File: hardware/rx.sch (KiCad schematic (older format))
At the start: 18 parts, among them J4 SMA, U22 TRF37A73, U23 SKY65404

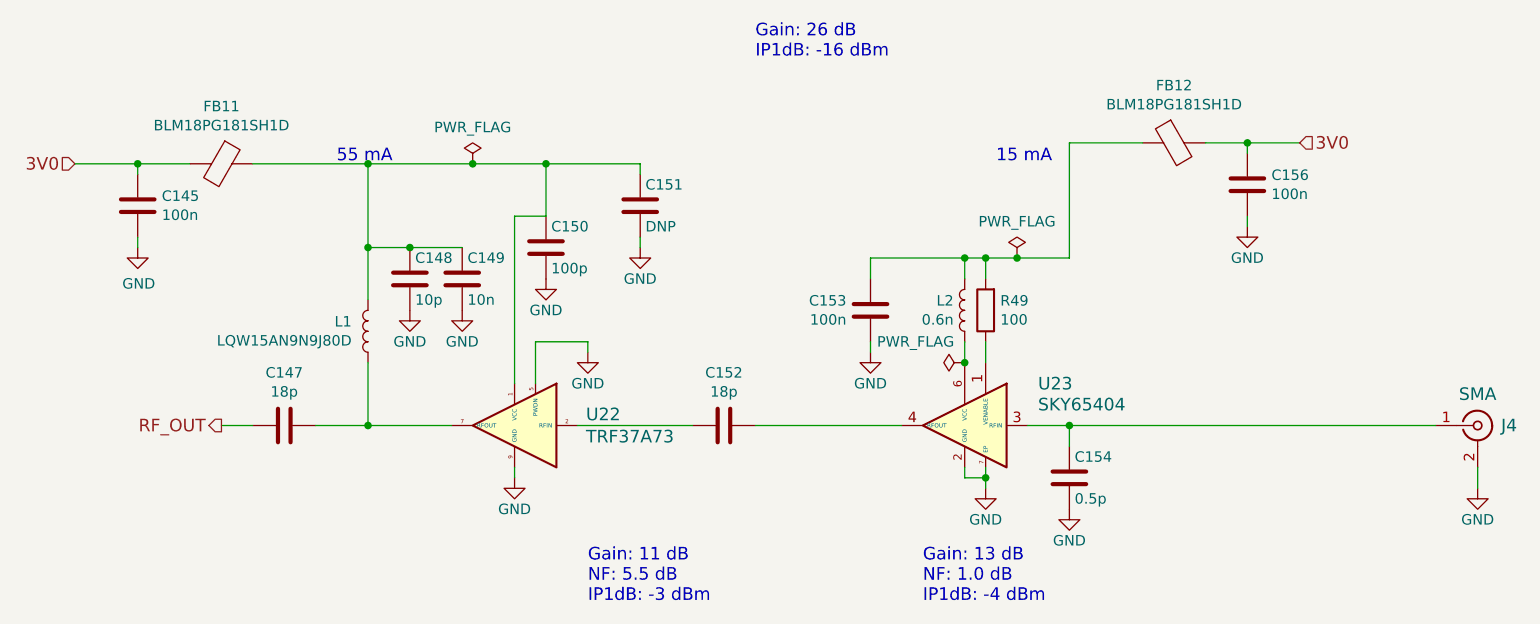
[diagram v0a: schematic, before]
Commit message: Completed receivers.
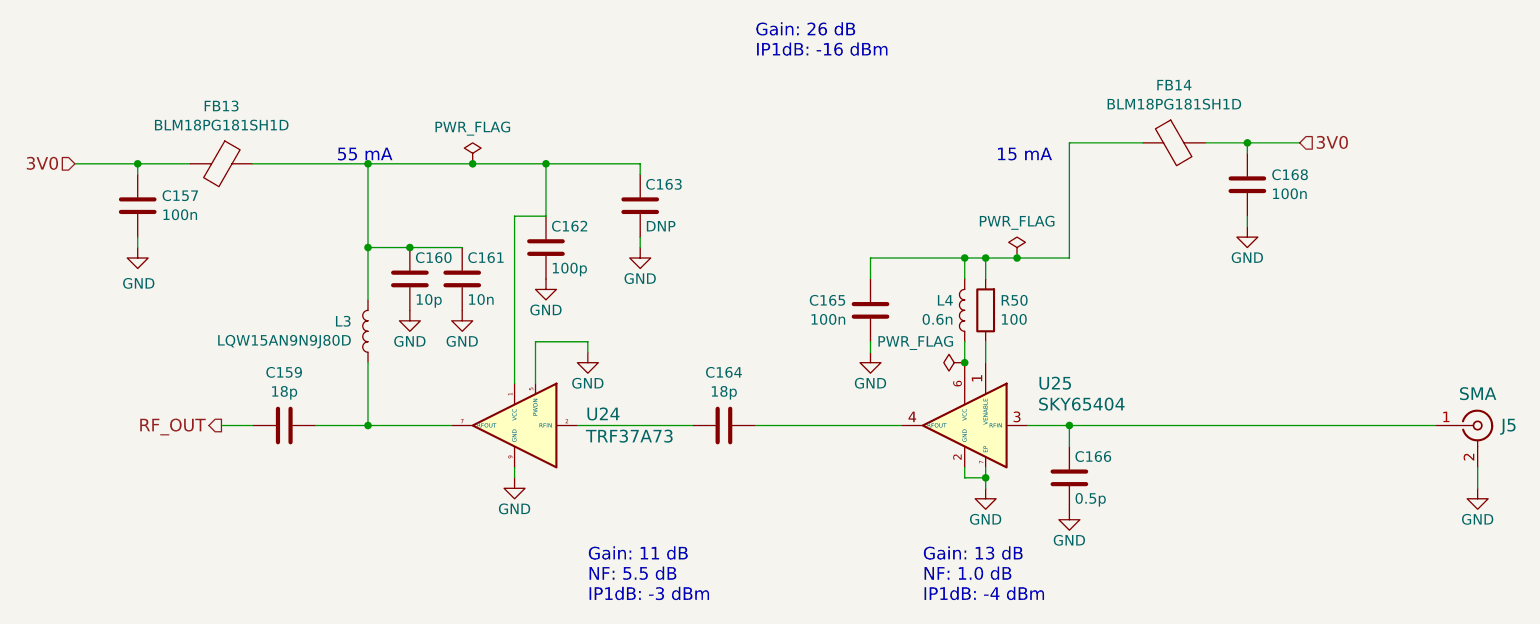
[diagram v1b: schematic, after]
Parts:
- C154: MFN C1005C0G1H0R5B050BA -> 500R07S0R5BV4T
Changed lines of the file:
@@
 $Descr A4 11693 8268
 encoding utf-8
-Sheet 6 10
+Sheet 7 10
 Title ""
 Date ""
@@
 AR Path="/59396B97/593BC199" Ref="U23"  Part="1"
 AR Path="/593D90BA/593BC199" Ref="U25"  Part="1"
-F 0 "U23" H 6550 4150 60  0000 R CNN
+F 0 "U25" H 6550 4150 60  0000 R CNN
 F 1 "SKY65404" H 6550 4050 60  0000 R CNN
 F 2 "Package_DFN_QFN:Skyworks_DFN-6-1EP_1.5x1.5mm_P0.5mm_EP0.7x1.2mm" H 6750 3950 60  0001 C CNN
@@
 AR Path="/59396B97/593BC25F" Ref="#PWR0158"  Part="1"
 AR Path="/593D90BA/593BC25F" Ref="#PWR0172"  Part="1"
-F 0 "#PWR0158" H 6800 4000 50  0001 C CNN
+F 0 "#PWR0172" H 6800 4000 50  0001 C CNN
 F 1 "GND" H 6800 4100 50  0000 C CNN
 F 2 "" H 6800 4250 60  0000 C CNN
@@
 AR Path="/59396B97/593BC396" Ref="R49"  Part="1"
 AR Path="/593D90BA/593BC396" Ref="R50"  Part="1"
-F 0 "R49" H 6730 3354 50  0000 R CNN
+F 0 "R50" H 6730 3354 50  0000 R CNN
 F 1 "100" H 6730 3445 50  0000 R CNN
 F 2 "Resistor_SMD:R_0402_1005Metric" V 6730 3400 30  0001 C CNN
@@
 AR Path="/59396B97/593BC695" Ref="L2"  Part="1"
 AR Path="/593D90BA/593BC695" Ref="L4"  Part="1"
-F 0 "L2" H 6753 3354 50  0000 L CNN
+F 0 "L4" H 6753 3354 50  0000 L CNN
 F 1 "0.6n" H 6753 3445 50  0000 L CNN
 F 2 "Inductor_SMD:L_0402_1005Metric" H 6700 3400 60  0001 C CNN
@@
 AR Path="/59396B97/593BC767" Ref="C153"  Part="1"
 AR Path="/593D90BA/593BC767" Ref="C165"  Part="1"
-F 0 "C153" H 6135 3446 50  0000 R CNN
+F 0 "C165" H 6135 3446 50  0000 R CNN
 F 1 "100n" H 6135 3355 50  0000 R CNN
 F 2 "Capacitor_SMD:C_0402_1005Metric" H 6288 3250 30  0001 C CNN
@@
 AR Path="/59396B97/593BC7DB" Ref="#PWR0157"  Part="1"
 AR Path="/593D90BA/593BC7DB" Ref="#PWR0171"  Part="1"
-F 0 "#PWR0157" H 6250 3350 50  0001 C CNN
+F 0 "#PWR0171" H 6250 3350 50  0001 C CNN
 F 1 "GND" H 6250 3450 50  0000 C CNN
 F 2 "" H 6250 3600 60  0000 C CNN
@@
 AR Path="/59396B97/593BCCCA" Ref="J4"  Part="1"
 AR Path="/593D90BA/593BCCCA" Ref="J5"  Part="1"
-F 0 "J4" H 9300 3950 60  0000 C CNN
+F 0 "J5" H 9300 3950 60  0000 C CNN
 F 1 "SMA" H 9150 4100 60  0000 C CNN
 F 2 "fmcw:CONSMA003.062" H 9150 3950 60  0001 C CNN
@@
 AR Path="/59396B97/593BCD59" Ref="#PWR0162"  Part="1"
 AR Path="/593D90BA/593BCD59" Ref="#PWR0176"  Part="1"
-F 0 "#PWR0162" H 9150 4000 50  0001 C CNN
+F 0 "#PWR0176" H 9150 4000 50  0001 C CNN
 F 1 "GND" H 9150 4100 50  0000 C CNN
 F 2 "" H 9150 4250 60  0000 C CNN
@@
 AR Path="/59396B97/593BCEBC" Ref="C154"  Part="1"
 AR Path="/593D90BA/593BCEBC" Ref="C166"  Part="1"
-F 0 "C154" H 7225 4300 50  0000 L CNN
+F 0 "C166" H 7225 4300 50  0000 L CNN
 F 1 "0.5p" H 7225 4100 50  0000 L CNN
 F 2 "Capacitor_SMD:C_0402_1005Metric" H 7238 4050 30  0001 C CNN
 F 3 "" H 7200 4200 60  0000 C CNN
-F 4 "C1005C0G1H0R5B050BA" H -1250 0   50  0001 C CNN "MFN"
+F 4 "500R07S0R5BV4T" H -1250 0   50  0001 C CNN "MFN"
 	1    7200 4200
 	1    0    0    -1
@@
 AR Path="/59396B97/593BCF37" Ref="#PWR0159"  Part="1"
 AR Path="/593D90BA/593BCF37" Ref="#PWR0173"  Part="1"
-F 0 "#PWR0159" H 7200 4100 50  0001 C CNN
+F 0 "#PWR0173" H 7200 4100 50  0001 C CNN
 F 1 "GND" H 7200 4200 50  0000 C CNN
 F 2 "" H 7200 4350 60  0000 C CNN
@@
 AR Path="/59396B97/593BD4EF" Ref="C152"  Part="1"
 AR Path="/593D90BA/593BD4EF" Ref="C164"  Part="1"
-F 0 "C152" V 5298 3950 50  0000 C CNN
+F 0 "C164" V 5298 3950 50  0000 C CNN
 F 1 "18p" V 5389 3950 50  0000 C CNN
 F 2 "Capacitor_SMD:C_0402_1005Metric" H 5588 3800 30  0001 C CNN
@@
 AR Path="/59396B97/593BD727" Ref="#PWR0153"  Part="1"
 AR Path="/593D90BA/593BD727" Ref="#PWR0167"  Part="1"
-F 0 "#PWR0153" H 4550 3950 50  0001 C CNN
+F 0 "#PWR0167" H 4550 3950 50  0001 C CNN
 F 1 "GND" H 4550 4050 50  0000 C CNN
 F 2 "" H 4550 4200 60  0000 C CNN
@@
 AR Path="/59396B97/593BD8E8" Ref="L1"  Part="1"
 AR Path="/593D90BA/593BD8E8" Ref="L3"  Part="1"
-F 0 "L1" H 3928 3454 50  0000 L CNN
+F 0 "L3" H 3928 3454 50  0000 L CNN
 F 1 "LQW15AN9N9J80D" H 3928 3545 50  0000 L CNN
 F 2 "Inductor_SMD:L_0402_1005Metric" H 3850 3500 60  0001 C CNN
@@
 AR Path="/59396B97/593BDA25" Ref="C148"  Part="1"
 AR Path="/593D90BA/593BDA25" Ref="C160"  Part="1"
-F 0 "C148" H 4075 3350 50  0000 L CNN
+F 0 "C160" H 4075 3350 50  0000 L CNN
 F 1 "10p" H 4075 3150 50  0000 L CNN
 F 2 "Capacitor_SMD:C_0402_1005Metric" H 4088 3100 30  0001 C CNN
@@
 AR Path="/59396B97/593BDABD" Ref="#PWR0151"  Part="1"
 AR Path="/593D90BA/593BDABD" Ref="#PWR0165"  Part="1"
-F 0 "#PWR0151" H 4050 3150 50  0001 C CNN
+F 0 "#PWR0165" H 4050 3150 50  0001 C CNN
 F 1 "GND" H 4050 3250 50  0000 C CNN
 F 2 "" H 4050 3400 60  0000 C CNN
@@
 AR Path="/59396B97/593BDF98" Ref="C147"  Part="1"
 AR Path="/593D90BA/593BDF98" Ref="C159"  Part="1"
-F 0 "C147" V 3198 3950 50  0000 C CNN
+F 0 "C159" V 3198 3950 50  0000 C CNN
 F 1 "18p" V 3289 3950 50  0000 C CNN
 F 2 "Capacitor_SMD:C_0402_1005Metric" H 3488 3800 30  0001 C CNN
@@
 AR Path="/593D90BA/59751767" Ref="FB13"  Part="1"
 AR Path="/59396B97/59751767" Ref="FB11"  Part="1"
-F 0 "FB11" V 2876 2700 50  0000 C CNN
+F 0 "FB13" V 2876 2700 50  0000 C CNN
 F 1 "BLM18PG181SH1D" V 2967 2700 50  0000 C CNN
 F 2 "Inductor_SMD:L_0603_1608Metric" H 3150 2700 60  0001 C CNN
@@
 AR Path="/593D90BA/59751D28" Ref="C163"  Part="1"
 AR Path="/59396B97/59751D28" Ref="C151"  Part="1"
-F 0 "C151" H 5175 3000 50  0000 L CNN
+F 0 "C163" H 5175 3000 50  0000 L CNN
 F 1 "DNP" H 5175 2800 50  0000 L CNN
 F 2 "Capacitor_SMD:C_0603_1608Metric" H 5188 2750 30  0001 C CNN
@@
 AR Path="/593D90BA/59751D9B" Ref="#PWR0170"  Part="1"
 AR Path="/59396B97/59751D9B" Ref="#PWR0156"  Part="1"
-F 0 "#PWR0156" H 5150 2850 50  0001 C CNN
+F 0 "#PWR0170" H 5150 2850 50  0001 C CNN
 F 1 "GND" H 5150 2950 50  0000 C CNN
 F 2 "" H 5150 3100 60  0000 C CNN
@@
 AR Path="/593D90BA/597527FA" Ref="FB14"  Part="1"
 AR Path="/59396B97/597527FA" Ref="FB12"  Part="1"
-F 0 "FB12" V 7426 2600 50  0000 C CNN
+F 0 "FB14" V 7426 2600 50  0000 C CNN
 F 1 "BLM18PG181SH1D" V 7517 2600 50  0000 C CNN
 F 2 "Inductor_SMD:L_0603_1608Metric" H 7700 2600 60  0001 C CNN
@@
 AR Path="/59396B97/59752CE4" Ref="#PWR0161"  Part="1"
 AR Path="/593D90BA/59752CE4" Ref="#PWR0175"  Part="1"
-F 0 "#PWR0161" H 8050 2750 50  0001 C CNN
+F 0 "#PWR0175" H 8050 2750 50  0001 C CNN
 F 1 "GND" H 8050 2850 50  0000 C CNN
 F 2 "" H 8050 3000 60  0000 C CNN
@@
 AR Path="/593D90BA/597605DF" Ref="U24"  Part="1"
 AR Path="/597605DF" Ref="U?"  Part="1"
-F 0 "U22" H 4409 4003 60  0000 R CNN
+F 0 "U24" H 4409 4003 60  0000 R CNN
 F 1 "TRF37A73" H 4409 3897 60  0000 R CNN
 F 2 "Package_SON:WSON-8-1EP_2x2mm_P0.5mm_EP0.9x1.6mm" H 4450 3900 60  0001 C CNN
@@
 AR Path="/59396B97/59761DBE" Ref="C150"  Part="1"
 AR Path="/593D90BA/59761DBE" Ref="C162"  Part="1"
-F 0 "C150" H 4725 3200 50  0000 L CNN
+F 0 "C162" H 4725 3200 50  0000 L CNN
 F 1 "100p" H 4725 3000 50  0000 L CNN
 F 2 "Capacitor_SMD:C_0402_1005Metric" H 4738 2950 30  0001 C CNN
@@
 AR Path="/59396B97/59761E7D" Ref="#PWR0154"  Part="1"
 AR Path="/593D90BA/59761E7D" Ref="#PWR0168"  Part="1"
-F 0 "#PWR0154" H 4700 3000 50  0001 C CNN
+F 0 "#PWR0168" H 4700 3000 50  0001 C CNN
 F 1 "GND" H 4700 3100 50  0000 C CNN
 F 2 "" H 4700 3250 60  0000 C CNN
@@
 AR Path="/59396B97/59762FC5" Ref="C149"  Part="1"
 AR Path="/593D90BA/59762FC5" Ref="C161"  Part="1"
-F 0 "C149" H 4325 3350 50  0000 L CNN
+F 0 "C161" H 4325 3350 50  0000 L CNN
 F 1 "10n" H 4325 3150 50  0000 L CNN
 F 2 "Capacitor_SMD:C_0402_1005Metric" H 4338 3100 30  0001 C CNN
@@
 AR Path="/59396B97/5976305E" Ref="#PWR0152"  Part="1"
 AR Path="/593D90BA/5976305E" Ref="#PWR0166"  Part="1"
-F 0 "#PWR0152" H 4300 3150 50  0001 C CNN
+F 0 "#PWR0166" H 4300 3150 50  0001 C CNN
 F 1 "GND" H 4300 3250 50  0000 C CNN
 F 2 "" H 4300 3400 60  0000 C CNN
@@
 AR Path="/59396B97/5CF2FC64" Ref="#FLG011"  Part="1"
 AR Path="/593D90BA/5CF2FC64" Ref="#FLG014"  Part="1"
-F 0 "#FLG011" H 4350 2775 50  0001 C CNN
+F 0 "#FLG014" H 4350 2775 50  0001 C CNN
 F 1 "PWR_FLAG" H 4350 2874 50  0000 C CNN
 F 2 "" H 4350 2700 50  0001 C CNN
@@
 AR Path="/59396B97/5CF2FCC1" Ref="#FLG013"  Part="1"
 AR Path="/593D90BA/5CF2FCC1" Ref="#FLG016"  Part="1"
-F 0 "#FLG013" H 6950 3225 50  0001 C CNN
+F 0 "#FLG016" H 6950 3225 50  0001 C CNN
 F 1 "PWR_FLAG" H 6950 3324 50  0000 C CNN
 F 2 "" H 6950 3150 50  0001 C CNN
@@
 AR Path="/59396B97/5CF3D956" Ref="#FLG012"  Part="1"
 AR Path="/593D90BA/5CF3D956" Ref="#FLG015"  Part="1"
-F 0 "#FLG012" H 6700 3725 50  0001 C CNN
+F 0 "#FLG015" H 6700 3725 50  0001 C CNN
 F 1 "PWR_FLAG" V 6800 3700 50  0000 L CNN
 F 2 "" H 6700 3650 50  0001 C CNN
@@
 AR Path="/59396B97/5C429467" Ref="#PWR0155"  Part="1"
 AR Path="/593D90BA/5C429467" Ref="#PWR0169"  Part="1"
-F 0 "#PWR0155" H 4900 3350 50  0001 C CNN
+F 0 "#PWR0169" H 4900 3350 50  0001 C CNN
 F 1 "GND" H 4900 3450 50  0000 C CNN
 F 2 "" H 4900 3600 60  0000 C CNN
@@
 AR Path="/59396B97/5C42C3BD" Ref="C156"  Part="1"
 AR Path="/593D90BA/5C42C3BD" Ref="C168"  Part="1"
-F 0 "C156" H 8165 2846 50  0000 L CNN
+F 0 "C168" H 8165 2846 50  0000 L CNN
 F 1 "100n" H 8165 2755 50  0000 L CNN
 F 2 "Capacitor_SMD:C_0402_1005Metric" H 8088 2650 30  0001 C CNN
@@
 AR Path="/59396B97/5C42DC20" Ref="C145"  Part="1"
 AR Path="/593D90BA/5C42DC20" Ref="C157"  Part="1"
-F 0 "C145" H 2865 2946 50  0000 L CNN
+F 0 "C157" H 2865 2946 50  0000 L CNN
 F 1 "100n" H 2865 2855 50  0000 L CNN
 F 2 "Capacitor_SMD:C_0402_1005Metric" H 2788 2750 30  0001 C CNN
@@
 AR Path="/59396B97/5C430750" Ref="#PWR0149"  Part="1"
 AR Path="/593D90BA/5C430750" Ref="#PWR0163"  Part="1"
-F 0 "#PWR0149" H 2750 2850 50  0001 C CNN
+F 0 "#PWR0163" H 2750 2850 50  0001 C CNN
 F 1 "GND" H 2755 2927 50  0000 C CNN
 F 2 "" H 2750 3100 50  0001 C CNN

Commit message: Filter FPGA code.
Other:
- note added: "Gain: 11 dB\nNF: 5.5 dB\nIP1dB: -3.5 dBm"
- note added: "Gain: 24 dB\nIP1dB: -16.5 dBm"
- note removed: "Gain: 11 dB\nNF: 5.5 dB\nIP1dB: -3 dBm"
- note removed: "Gain: 26 dB\nIP1dB: -16 dBm"
